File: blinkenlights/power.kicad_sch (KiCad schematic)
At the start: 30 parts, among them J301 Conn_01x01_Female, J302 Conn_01x01_Female, J303 Conn_01x01_Female, U301 AP62250Z6, U302 AP62250Z6

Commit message: Start work on blinkenlights pcb
- This is mostly for the general layout and physical size of the board;
  all the components are placed on the back so the pin numbers will line
  up properly on the DIN connectors.
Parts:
- J301, J302, J303: footprint (none) -> 68komputer-common:DELTRON-571-0x00
- L301, L302: footprint (none) -> Inductor_SMD:L_Taiyo-Yuden_NR-60xx; MPN (none) -> NR6028T2R2N
- R301, R302, R303, R304, R305, R306, R307: footprint (none) -> Resistor_SMD:R_0805_2012Metric
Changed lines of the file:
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@@
   (paper "A4")
   (junction (at 80.01 144.78) (diameter 0) (color 0 0 0 0))
+  (junction (at 90.17 137.16) (diameter 0) (color 0 0 0 0))
+  (junction (at 80.01 178.591) (diameter 0) (color 0 0 0 0))
+  (junction (at 100.965 137.16) (diameter 0) (color 0 0 0 0))
+  (junction (at 90.17 170.971) (diameter 0) (color 0 0 0 0))
+  (junction (at 194.31 157.48) (diameter 0) (color 0 0 0 0))
+  (junction (at 100.965 170.971) (diameter 0) (color 0 0 0 0))
+  (junction (at 80.01 170.971) (diameter 0) (color 0 0 0 0))
+  (junction (at 184.15 152.4) (diameter 0) (color 0 0 0 0))
+  (junction (at 110.49 176.051) (diameter 0) (color 0 0 0 0))
+  (junction (at 100.965 142.24) (diameter 0) (color 0 0 0 0))
+  (junction (at 184.15 157.48) (diameter 0) (color 0 0 0 0))
+  (junction (at 24.13 139.7) (diameter 0) (color 0 0 0 0))
+  (junction (at 276.86 120.65) (diameter 0) (color 0 0 0 0))
+  (junction (at 110.49 142.24) (diameter 0) (color 0 0 0 0))
+  (junction (at 80.01 137.16) (diameter 0) (color 0 0 0 0))
+  (junction (at 110.49 170.971) (diameter 0) (color 0 0 0 0))
+  (junction (at 24.13 173.511) (diameter 0) (color 0 0 0 0))
+  (junction (at 194.31 152.4) (diameter 0) (color 0 0 0 0))
+  (junction (at 276.86 111.76) (diameter 0) (color 0 0 0 0))
   (junction (at 100.965 176.051) (diameter 0) (color 0 0 0 0))
-  (junction (at 100.965 142.24) (diameter 0) (color 0 0 0 0))
-  (junction (at 24.13 173.511) (diameter 0) (color 0 0 0 0))
-  (junction (at 276.86 111.76) (diameter 0) (color 0 0 0 0))
-  (junction (at 276.86 120.65) (diameter 0) (color 0 0 0 0))
-  (junction (at 194.31 152.4) (diameter 0) (color 0 0 0 0))
-  (junction (at 110.49 176.051) (diameter 0) (color 0 0 0 0))
-  (junction (at 90.17 170.971) (diameter 0) (color 0 0 0 0))
-  (junction (at 24.13 139.7) (diameter 0) (color 0 0 0 0))
-  (junction (at 110.49 170.971) (diameter 0) (color 0 0 0 0))
-  (junction (at 184.15 157.48) (diameter 0) (color 0 0 0 0))
-  (junction (at 90.17 137.16) (diameter 0) (color 0 0 0 0))
-  (junction (at 100.965 137.16) (diameter 0) (color 0 0 0 0))
+  (junction (at 66.04 170.971) (diameter 0) (color 0 0 0 0))
   (junction (at 66.04 137.16) (diameter 0) (color 0 0 0 0))
-  (junction (at 100.965 170.971) (diameter 0) (color 0 0 0 0))
-  (junction (at 184.15 152.4) (diameter 0) (color 0 0 0 0))
-  (junction (at 80.01 137.16) (diameter 0) (color 0 0 0 0))
-  (junction (at 80.01 178.591) (diameter 0) (color 0 0 0 0))
-  (junction (at 66.04 170.971) (diameter 0) (color 0 0 0 0))
-  (junction (at 80.01 170.971) (diameter 0) (color 0 0 0 0))
-  (junction (at 194.31 157.48) (diameter 0) (color 0 0 0 0))
-  (junction (at 110.49 142.24) (diameter 0) (color 0 0 0 0))
   (wire (pts (xy 77.47 170.971) (xy 80.01 170.971))
     (stroke (width 0) (type default) (color 0 0 0 0))
@@
     (property "Reference" "R307" (id 0) (at 263.525 98.1669 90))
     (property "Value" "300R" (id 1) (at 263.525 100.942 90))
-    (property "Footprint" "" (id 2) (at 263.525 102.87 0)
+    (property "Footprint" "Resistor_SMD:R_0805_2012Metric" (id 2) (at 263.525 102.87 0)
       (effects (font (size 1.27 1.27)) hide)
     )
@@
     (property "Reference" "L302" (id 0) (at 74.93 132.8124 90))
     (property "Value" "2.2µH" (id 1) (at 74.93 135.5875 90))
-    (property "Footprint" "" (id 2) (at 74.93 137.16 0)
+    (property "Footprint" "Inductor_SMD:L_Taiyo-Yuden_NR-60xx" (id 2) (at 74.93 137.16 0)
       (effects (font (size 1.27 1.27)) hide)
     )
     (property "Datasheet" "~" (id 3) (at 74.93 137.16 0)
+      (effects (font (size 1.27 1.27)) hide)
+    )
+    (property "MPN" "NR6028T2R2N" (id 4) (at 74.93 137.16 90)
       (effects (font (size 1.27 1.27)) hide)
     )
@@
     (property "Reference" "L301" (id 0) (at 74.93 166.6234 90))
     (property "Value" "2.2µH" (id 1) (at 74.93 169.3985 90))
-    (property "Footprint" "" (id 2) (at 74.93 170.971 0)
+    (property "Footprint" "Inductor_SMD:L_Taiyo-Yuden_NR-60xx" (id 2) (at 74.93 170.971 0)
       (effects (font (size 1.27 1.27)) hide)
     )
     (property "Datasheet" "~" (id 3) (at 74.93 170.971 0)
+      (effects (font (size 1.27 1.27)) hide)
+    )
+    (property "MPN" "NR6028T2R2N" (id 4) (at 74.93 170.971 90)
       (effects (font (size 1.27 1.27)) hide)
     )
@@
     (property "Reference" "J302" (id 0) (at 270.548 141.6263 0))
     (property "Value" "Conn_01x01_Female" (id 1) (at 270.548 144.4014 0))
-    (property "Footprint" "" (id 2) (at 273.05 146.05 0)
+    (property "Footprint" "68komputer-common:DELTRON-571-0x00" (id 2) (at 273.05 146.05 0)
       (effects (font (size 1.27 1.27)) hide)
     )
@@
       (effects (font (size 1.27 1.27)) (justify left))
     )
-    (property "Footprint" "" (id 2) (at 80.01 181.131 0)
+    (property "Footprint" "Resistor_SMD:R_0805_2012Metric" (id 2) (at 80.01 181.131 0)
       (effects (font (size 1.27 1.27)) hide)
     )
@@
       (effects (font (size 1.27 1.27)) (justify left))
     )
-    (property "Footprint" "" (id 2) (at 80.01 147.32 0)
+    (property "Footprint" "Resistor_SMD:R_0805_2012Metric" (id 2) (at 80.01 147.32 0)
       (effects (font (size 1.27 1.27)) hide)
     )
@@
     (property "Reference" "R304" (id 0) (at 263.525 115.9469 90))
     (property "Value" "4k7" (id 1) (at 263.525 118.722 90))
-    (property "Footprint" "" (id 2) (at 263.525 120.65 0)
+    (property "Footprint" "Resistor_SMD:R_0805_2012Metric" (id 2) (at 263.525 120.65 0)
       (effects (font (size 1.27 1.27)) hide)
     )
@@
     (property "Reference" "J301" (id 0) (at 270.548 135.2763 0))
     (property "Value" "Conn_01x01_Female" (id 1) (at 270.548 138.0514 0))
-    (property "Footprint" "" (id 2) (at 273.05 139.7 0)
+    (property "Footprint" "68komputer-common:DELTRON-571-0x00" (id 2) (at 273.05 139.7 0)
       (effects (font (size 1.27 1.27)) hide)
     )
@@
     (property "Reference" "J303" (id 0) (at 270.548 147.9763 0))
     (property "Value" "Conn_01x01_Female" (id 1) (at 270.548 150.7514 0))
-    (property "Footprint" "" (id 2) (at 273.05 152.4 0)
+    (property "Footprint" "68komputer-common:DELTRON-571-0x00" (id 2) (at 273.05 152.4 0)
       (effects (font (size 1.27 1.27)) hide)
     )
@@
     (property "Reference" "R303" (id 0) (at 263.525 107.0569 90))
     (property "Value" "300R" (id 1) (at 263.525 109.832 90))
-    (property "Footprint" "" (id 2) (at 263.525 111.76 0)
+    (property "Footprint" "Resistor_SMD:R_0805_2012Metric" (id 2) (at 263.525 111.76 0)
       (effects (font (size 1.27 1.27)) hide)
     )
@@
       (effects (font (size 1.27 1.27)) (justify left))
     )
-    (property "Footprint" "" (id 2) (at 80.01 139.7 0)
+    (property "Footprint" "Resistor_SMD:R_0805_2012Metric" (id 2) (at 80.01 139.7 0)
       (effects (font (size 1.27 1.27)) hide)
     )
@@
       (effects (font (size 1.27 1.27)) (justify left))
     )
-    (property "Footprint" "" (id 2) (at 80.01 173.511 0)
-      (effects (font (size 1.27 1.27)) hide)
-    )
+    (property "Footprint" "Resistor_SMD:R_0805_2012Metric" (id 2) (at 80.01 173.511 0)
+      (effects (font (size 1.27 1.27)) hide)
+    )

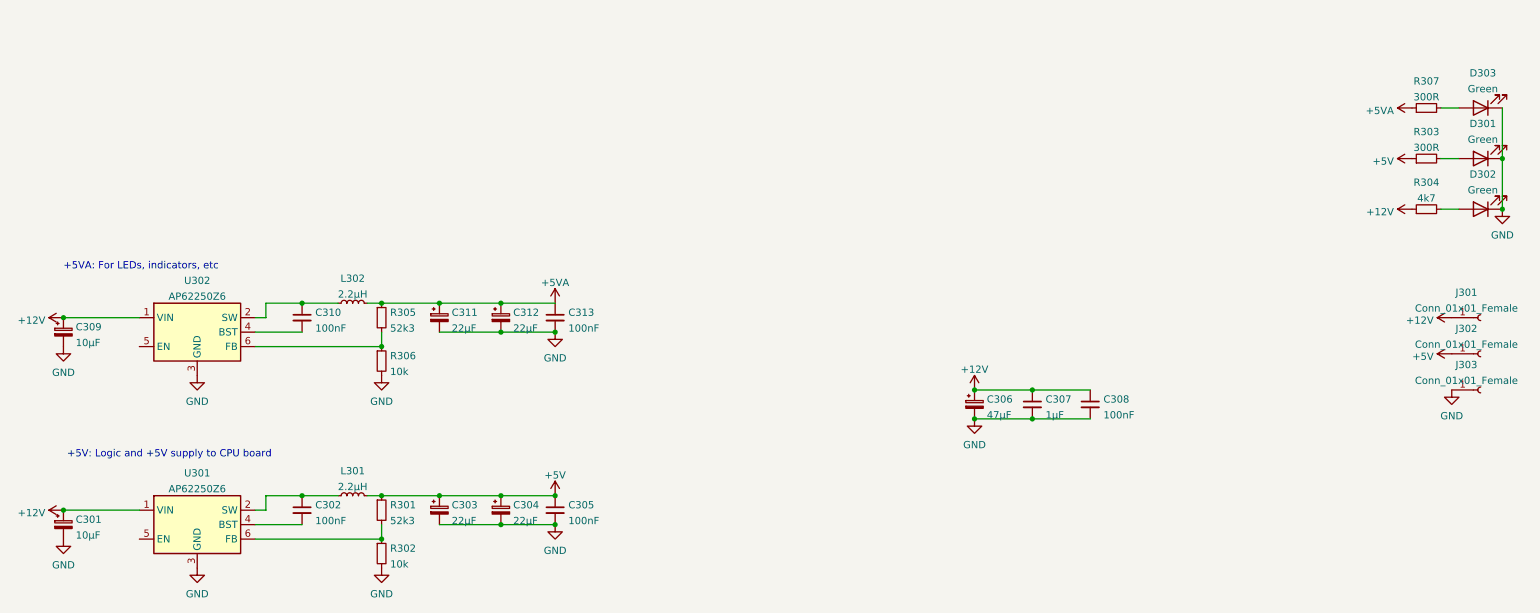
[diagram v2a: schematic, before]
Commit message: Rework blinkenlights board
- Removed ROMs, GALs and so forth from the blinkenlights board and
  simplified the power distribution significantly. This is in
  preparation for simply placing a big ass microcontroller that allows
  us to perform bus transactions manually (to load bootstrap programs,
  for example) on the system.
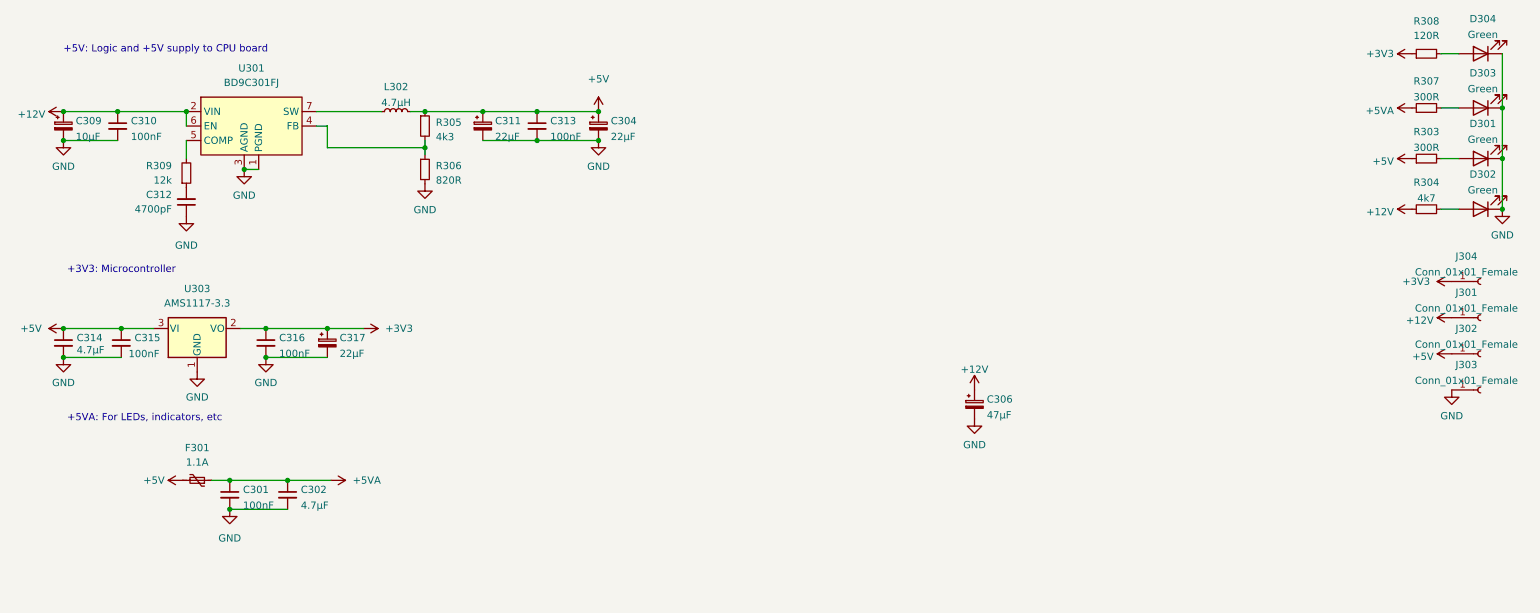
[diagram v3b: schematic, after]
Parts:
- removed C301: 10µF, Capacitor_Tantalum_SMD:CP_EIA-3528-21_Kemet-B, symbol Device:C_Polarized_Small
- removed C303, C312: 22µF, Capacitor_Tantalum_SMD:CP_EIA-3528-21_Kemet-B, symbol Device:C_Polarized_Small
- removed C305, C308: 100nF, Capacitor_SMD:C_0805_2012Metric, symbol Device:C_Small
- removed C307: 1µF, Capacitor_SMD:C_0805_2012Metric, symbol Device:C_Small
- removed L301: 2.2µH, Inductor_SMD:L_Taiyo-Yuden_NR-60xx, symbol Device:L_Small
- removed R301: 52k3, Resistor_SMD:R_0805_2012Metric, symbol Device:R_Small
- removed R302: 10k, Resistor_SMD:R_0805_2012Metric, symbol Device:R_Small
- removed U301, U302: AP62250Z6, Package_TO_SOT_SMD:SOT-563, symbol Regulator_Switching:AP62250Z6
- added C301, C315, C316: 100nF, Capacitor_SMD:C_0805_2012Metric, symbol Device:C_Small
- added C312: 4700pF, Capacitor_SMD:C_0805_2012Metric, symbol Device:C_Small
- added C314: 4.7µF, Capacitor_SMD:C_0805_2012Metric, symbol Device:C_Small
- added C317: 22µF, Capacitor_Tantalum_SMD:CP_EIA-3528-21_Kemet-B, symbol Device:C_Polarized_Small
- added D304: Green, LED_SMD:LED_0805_2012Metric, symbol Device:LED
- added F301: 1.1A, Fuse:Fuse_Bourns_MF-SM_7.98x5.44mm, symbol Device:Polyfuse_Small
- added J304: Conn_01x01_Female, 68komputer-common:DELTRON-571-0x00, symbol Connector:Conn_01x01_Female
- added R308: 120R, Resistor_SMD:R_0805_2012Metric, symbol Device:R_Small
- added R309: 12k, Resistor_SMD:R_0805_2012Metric, symbol Device:R_Small
- added U301: BD9C301FJ, Package_SO:SOP-8_3.9x4.9mm_P1.27mm, symbol 68komputer-common:BD9C301FJ
- added U303: AMS1117-3.3, Package_TO_SOT_SMD:SOT-223-3_TabPin2, symbol Regulator_Linear:AMS1117-3.3
- C302: value 100nF -> 4.7µF
- L302: value 2.2µH -> 4.7µH; footprint Inductor_SMD:L_Taiyo-Yuden_NR-60xx -> Inductor_SMD:L_Taiyo-Yuden_NR-80xx_HandSoldering; MPN NR6028T2R2N -> NRS8040T4R7NJGJ
- R305: value 52k3 -> 4k3
- R306: value 10k -> 820R
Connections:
- net +12V: now also C310.1, U301.2 (VIN), U301.6 (EN)
- net +5V: now also C311.1, C313.1, L302.2, R305.1, C314.1, C315.1, F301.2, U303.3 (VI)
- net +5VA: now also C302.1, C301.1, F301.1; no longer C311.1, C313.1, L302.2, R305.1
- net GND: now also C302.2, C310.2, C301.2, C312.1, C314.2, C315.2, C316.2, C317.2, D304.1 (K), U301.1 (PGND), U301.3 (AGND), U303.1 (GND)
- net at L302.1: now also U301.7 (SW), U301.8 (SW); no longer C310.1
- net at R305.2, R306.1: now also U301.4 (FB)
- new net: D304.2 (A), R308.2
- new net: C312.2, R309.1
- new net: R309.2, U301.5 (COMP)
- new net +3V3: C316.1, C317.1, J304.1 (Pin_1), R308.1, U303.2 (VO)
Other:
- note added: "+3V3: Microcontroller"
- moved on the sheet: C304, C309, C311, C313, L302, R305, R306

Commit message: Added Teensy, logic probe ports to blinkenlights
- A teensy 4.0 is on board connected to the IO expanders (and directly,
  the /HALT line, so it can single step the CPU on request) rather than
  expecting an external connection.

- Routed all bus signals to the logic analyzer connectors. They're meant
  to connect to a 16700-series pod connector on a 0.1" spacing, with 16
  signal lines, and one clock (CLK) with all other pins tied to ground.
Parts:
- removed C314: 4.7µF, Capacitor_SMD:C_0805_2012Metric, symbol Device:C_Small
- removed C315: 100nF, Capacitor_SMD:C_0805_2012Metric, symbol Device:C_Small
- removed J304: Conn_01x01_Female, 68komputer-common:DELTRON-571-0x00, symbol Connector:Conn_01x01_Female
- removed U303: AMS1117-3.3, Package_TO_SOT_SMD:SOT-223-3_TabPin2, symbol Regulator_Linear:AMS1117-3.3
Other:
- note added: "Provided by Teensy"
- moved on the sheet: C316, C317

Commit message: Some more direct IOs for blinkenlights
- /DTACK, /BERR, AS and R/W can be directly read/driven by Teensy GPIO;
  this should allow us to do bus transactions much faster since we can
  prepare the SPI transactions to set up the bus values, then control
  the bus timings most accurately.

- Fixed up a few incorrect pin directions for symbols used in the
  blinkenlights board
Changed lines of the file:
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@@
   (junction (at 276.86 120.65) (diameter 0) (color 0 0 0 0)
   )
+  (junction (at 257.81 139.7) (diameter 0) (color 0 0 0 0)
+  )
   (wire (pts (xy 24.13 108.585) (xy 33.655 108.585))
     (stroke (width 0) (type default) (color 0 0 0 0))
@@
     (stroke (width 0) (type default) (color 0 0 0 0))
   )
+  (wire (pts (xy 255.27 139.7) (xy 257.81 139.7))
+    (stroke (width 0) (type default) (color 0 0 0 0))
+  )
   (wire (pts (xy 266.065 102.87) (xy 269.24 102.87))
     (stroke (width 0) (type default) (color 0 0 0 0))
@@
   )
   (wire (pts (xy 68.58 103.505) (xy 80.01 103.505))
+    (stroke (width 0) (type default) (color 0 0 0 0))
+  )
+  (wire (pts (xy 257.81 139.7) (xy 267.97 139.7))
     (stroke (width 0) (type default) (color 0 0 0 0))
   )
@@
     (pin "1")
     (pin "2")
+  )
+  (symbol (lib_id "power:PWR_FLAG") (at 107.315 103.505 0) (unit 1)
+    (in_bom yes) (on_board yes) (fields_autoplaced)
+    (property "Reference" "#FLG0103" (id 0) (at 107.315 101.6 0)
+      (effects (font (size 1.27 1.27)) hide)
+    )
+    (property "Value" "PWR_FLAG" (id 1) (at 107.315 97.79 0))
+    (property "Footprint" "" (id 2) (at 107.315 103.505 0)
+      (effects (font (size 1.27 1.27)) hide)
+    )
+    (property "Datasheet" "~" (id 3) (at 107.315 103.505 0)
+      (effects (font (size 1.27 1.27)) hide)
+    )
+    (pin "1")
   )
   (symbol (lib_id "Device:C_Polarized_Small") (at 97.79 106.045 0) (unit 1)
@@
     (pin "1")
   )
+  (symbol (lib_id "power:PWR_FLAG") (at 257.81 139.7 0) (unit 1)
+    (in_bom yes) (on_board yes) (fields_autoplaced)
+    (property "Reference" "#FLG0102" (id 0) (at 257.81 137.795 0)
+      (effects (font (size 1.27 1.27)) hide)
+    )
+    (property "Value" "PWR_FLAG" (id 1) (at 257.81 134.62 0))
+    (property "Footprint" "" (id 2) (at 257.81 139.7 0)
+      (effects (font (size 1.27 1.27)) hide)
+    )
+    (property "Datasheet" "~" (id 3) (at 257.81 139.7 0)
+      (effects (font (size 1.27 1.27)) hide)
+    )
+    (pin "1")
+  )
   (symbol (lib_id "power:+5V") (at 267.97 146.05 90) (unit 1)
     (in_bom yes) (on_board yes) (fields_autoplaced)
@@
     (pin "2")
   )
-  (symbol (lib_id "power:+12V") (at 267.97 139.7 90) (unit 1)
-    (in_bom yes) (on_board yes) (fields_autoplaced)
-    (property "Reference" "#PWR0312" (id 0) (at 271.78 139.7 0)
-      (effects (font (size 1.27 1.27)) hide)
-    )
-    (property "Value" "+12V" (id 1) (at 264.795 140.179 90)
-      (effects (font (size 1.27 1.27)) (justify left))
-    )
-    (property "Footprint" "" (id 2) (at 267.97 139.7 0)
-      (effects (font (size 1.27 1.27)) hide)
-    )
-    (property "Datasheet" "" (id 3) (at 267.97 139.7 0)
+  (symbol (lib_id "power:+12V") (at 255.27 139.7 90) (unit 1)
+    (in_bom yes) (on_board yes) (fields_autoplaced)
+    (property "Reference" "#PWR0312" (id 0) (at 259.08 139.7 0)
+      (effects (font (size 1.27 1.27)) hide)
+    )
+    (property "Value" "+12V" (id 1) (at 252.095 140.179 90)
+      (effects (font (size 1.27 1.27)) (justify left))
+    )
+    (property "Footprint" "" (id 2) (at 255.27 139.7 0)
+      (effects (font (size 1.27 1.27)) hide)
+    )
+    (property "Datasheet" "" (id 3) (at 255.27 139.7 0)
       (effects (font (size 1.27 1.27)) hide)
     )
@@
     (pin "2")
   )
+  (symbol (lib_id "power:PWR_FLAG") (at 63.5 168.275 0) (unit 1)
+    (in_bom yes) (on_board yes) (fields_autoplaced)
+    (property "Reference" "#FLG0101" (id 0) (at 63.5 166.37 0)
+      (effects (font (size 1.27 1.27)) hide)
+    )
+    (property "Value" "PWR_FLAG" (id 1) (at 63.5 162.56 0))
+    (property "Footprint" "" (id 2) (at 63.5 168.275 0)
+      (effects (font (size 1.27 1.27)) hide)
+    )
+    (property "Datasheet" "~" (id 3) (at 63.5 168.275 0)
+      (effects (font (size 1.27 1.27)) hide)
+    )
+    (pin "1")
+  )
   (symbol (lib_id "Device:R_Small") (at 45.72 114.3 0) (mirror x) (unit 1)
